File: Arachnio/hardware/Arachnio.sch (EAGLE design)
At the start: 62 parts, among them J5 HEAD17-NOSS, J6 HEAD17-NOSS, Q1 8MHz, T1 FDN340P/PMV48XP, U1 ATMEGA32U4-XUMU, U2 AP2111HA-3.3, U3 ZLDO1117-5.0, U5 ESP8266EX, U6 SPI_FLASH, Y1 26 MHz/10 pF

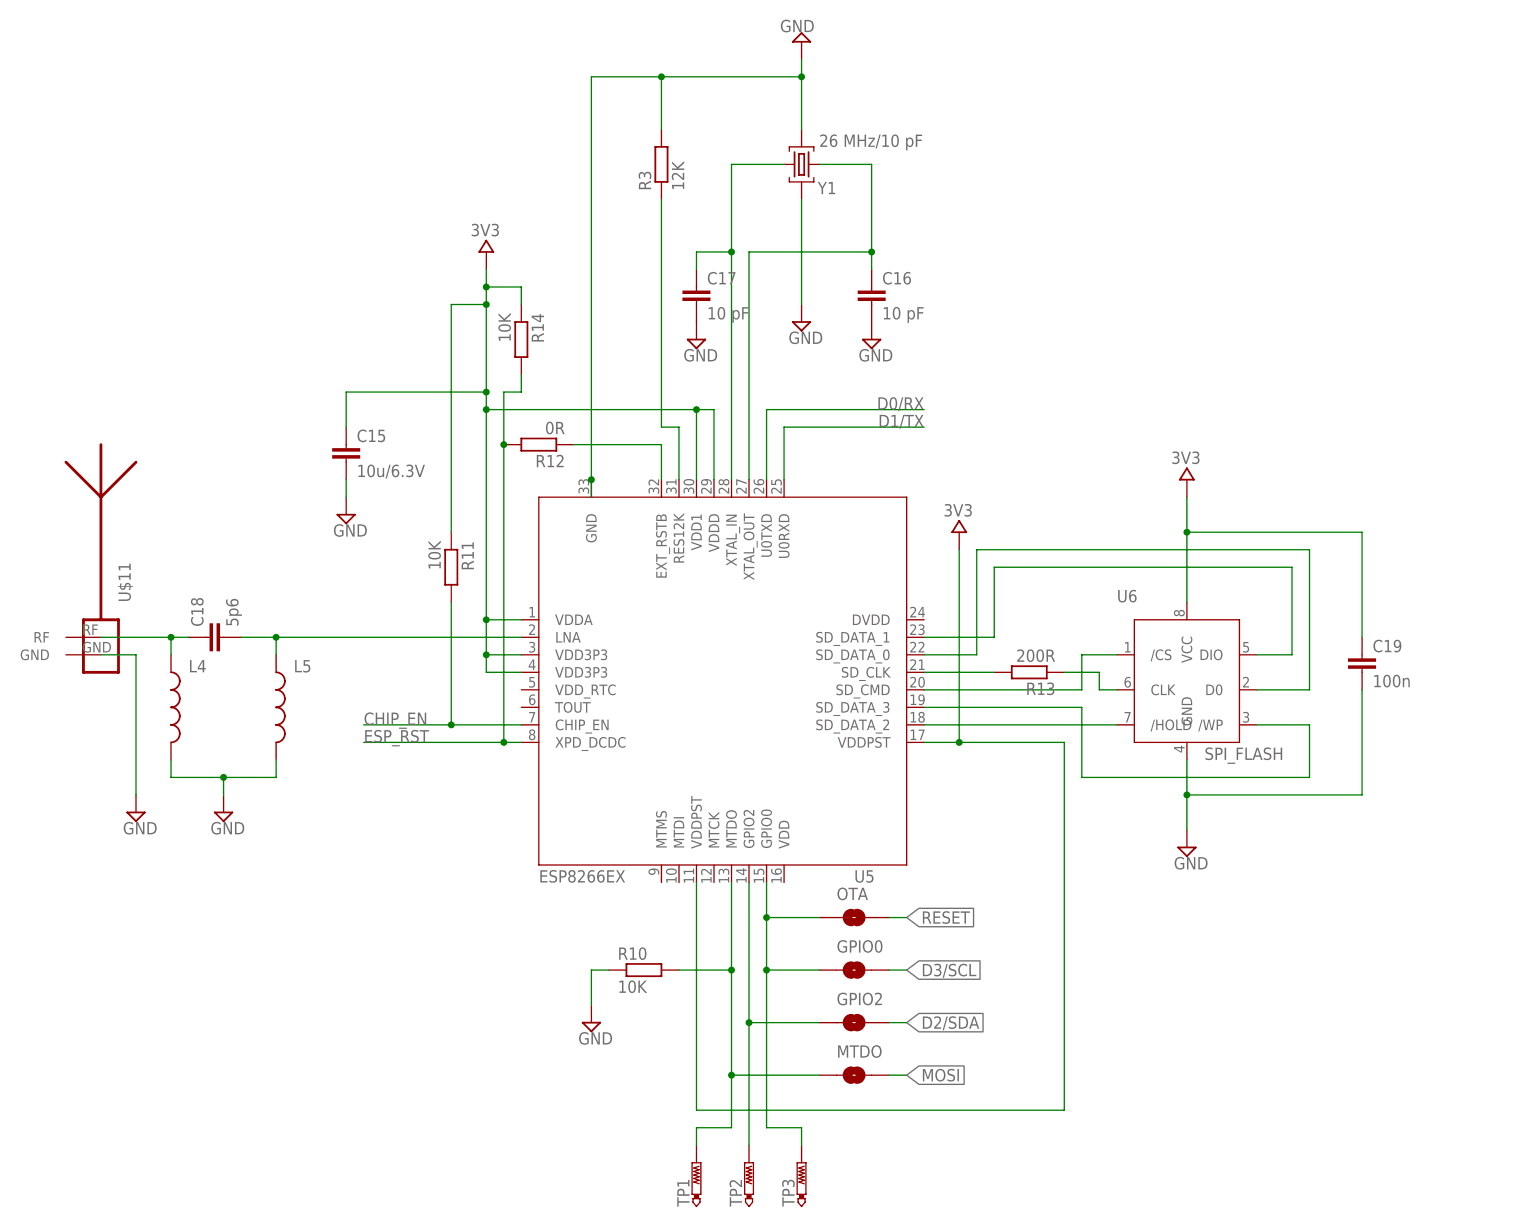
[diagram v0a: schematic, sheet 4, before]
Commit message: ﻿Added 3 new decoupling caps to the ESP8266 # Please enter the commit message for your changes. Lines starting # with '#' will be ignored, and an empty message aborts the commit. # On branch decoupling # Changes to be committed: #	modified:   Arachnio/hardware/Arachnio.brd #	modified:   Arachnio/hardware/Arachnio.sch #
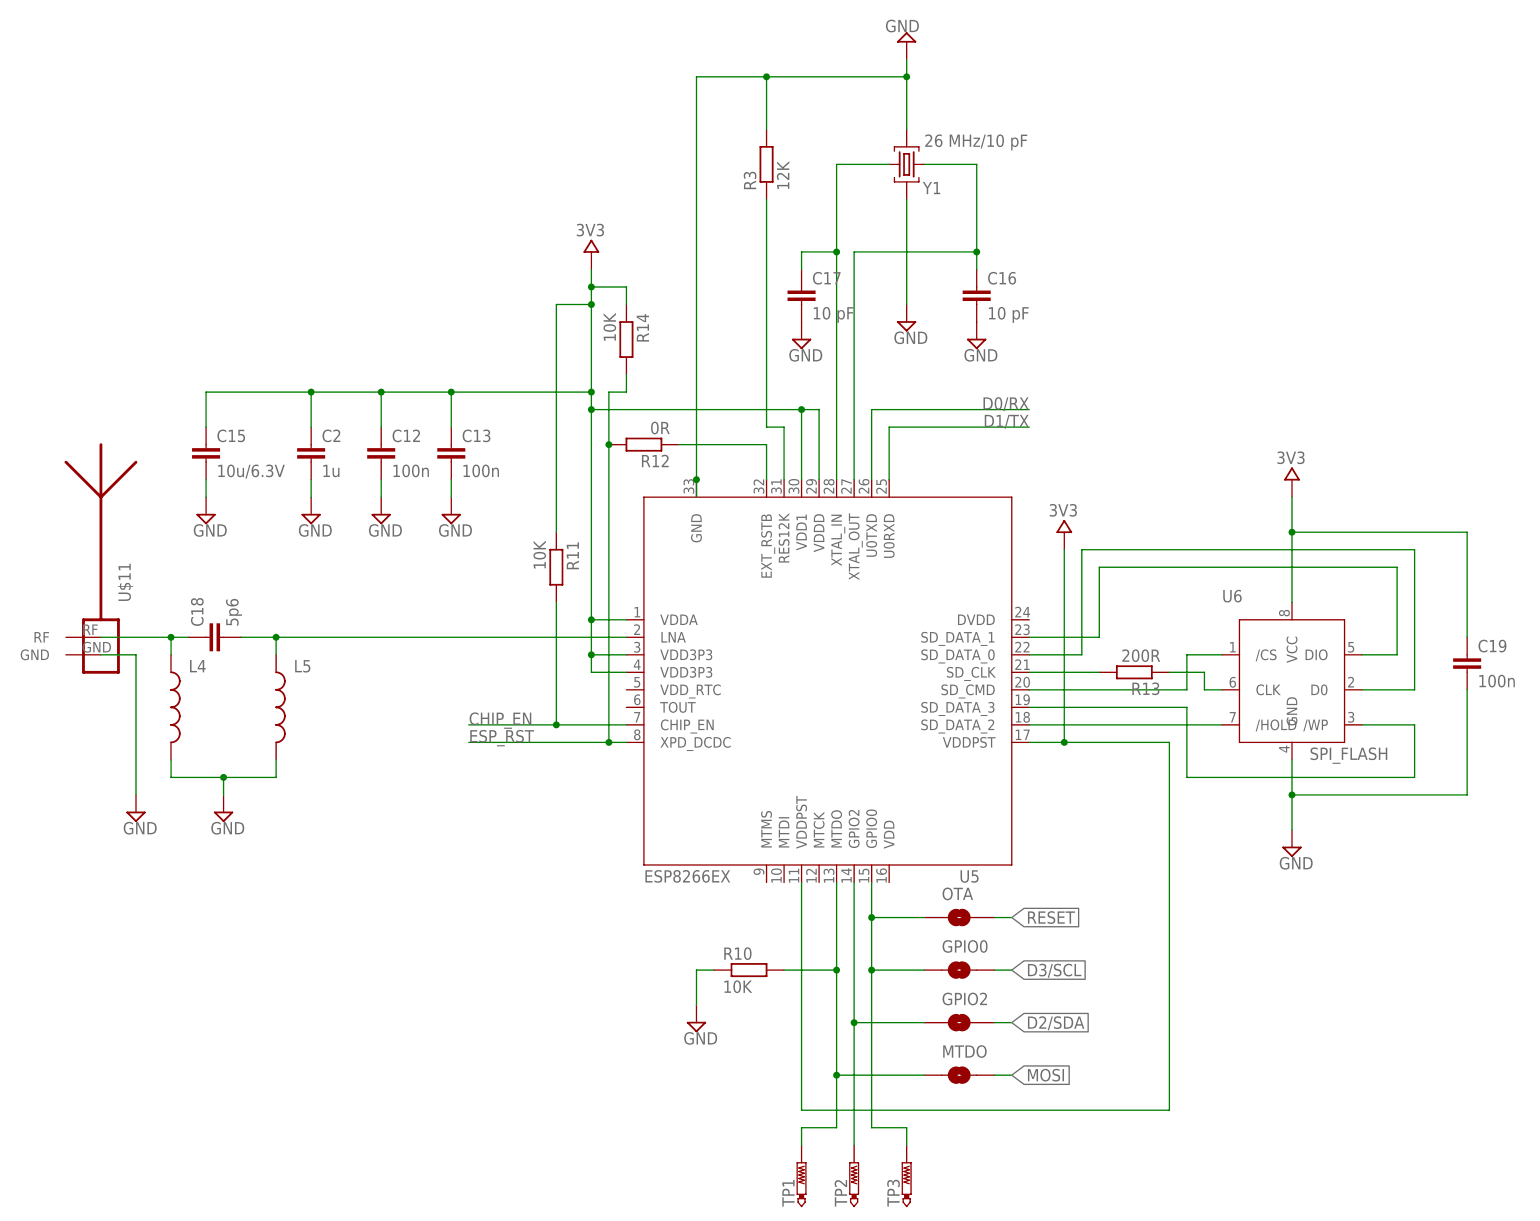
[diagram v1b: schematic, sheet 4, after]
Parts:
- added C12, C13: 100n, resistor:C-EUC0603
- added C2: 1u, resistor:C-EUC0603
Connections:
- net 3V3: now also C12.1, C13.1, C2.1
- net GND: now also C12.2, C13.2, C2.2
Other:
- moved on the sheet: C15, C16, C17, C19, GPIO0, GPIO2, MTDO, OTA, R10, R11, R12, R13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

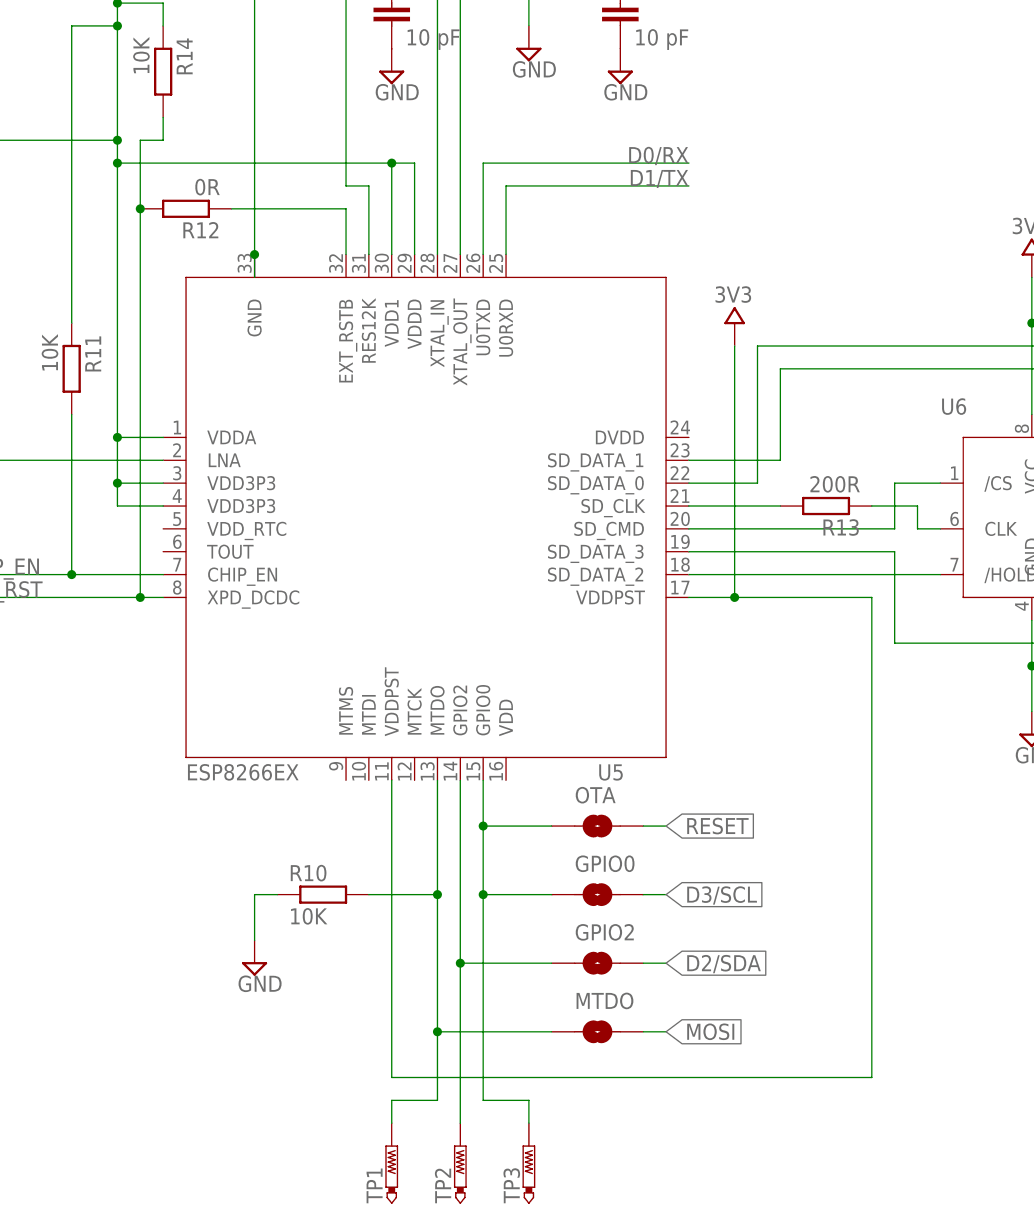
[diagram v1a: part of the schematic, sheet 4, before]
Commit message: -- Fixed ground plane issues -- Connected USB shield to ground -- Simplified boot select by tying MTDO and GPIO2 low and high, respectively -- Removed test points for MTDO and GPIO2 -- Replaced 0R resistor with NC by trace solder jumper -- Replaced GPIO2 and OTA jumpers with a single 3-way NO solder jumper
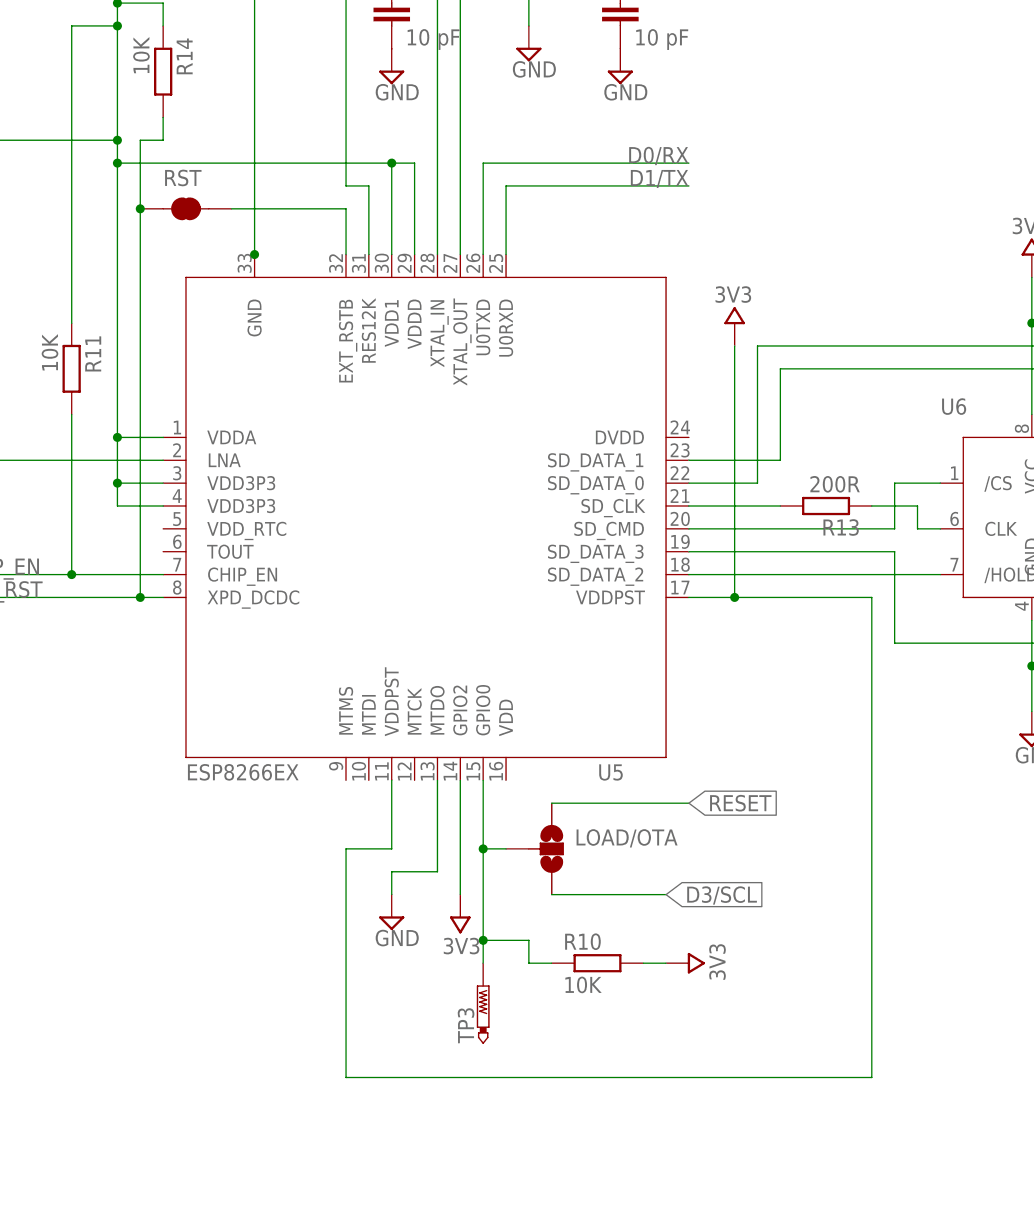
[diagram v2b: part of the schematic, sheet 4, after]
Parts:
- removed GPIO0, GPIO2, MTDO, OTA: JUMPER-PAD-2-NOYES_SILK, SparkFun-Passives:JUMPER-PAD-2-NOYES_SILK
- removed R12: 0R, resistor:R-EU_R0603
- removed TP1, TP2: PTR1TP15SQ, testpad:PTR1TP15SQ
- added LOAD/OTA: JUMPER-PAD-3-NOYES_SILK, SparkFun-Passives:JUMPER-PAD-3-NOYES_SILK
- added RST: JUMPER-PAD-2-NC_BY_TRACE, SparkFun-Passives:JUMPER-PAD-2-NC_BY_TRACE
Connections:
- removed net N$1: MTDO.1, R10.2, TP1.TP, U5.MTDO
- removed net N$5: GPIO2.1, TP2.TP, U5.GPIO2
- net 3V3: now also R10.2, U5.GPIO2
- net D2/SDA: no longer GPIO2.2
- net D3/SCL: now also LOAD/OTA.3; no longer GPIO0.2
- net ESP_RST: now also RST.1; no longer R12.2
- net GND: now also CN1.SHIELD@0, CN1.SHIELD@1, CN1.SHIELD@2, CN1.SHIELD@3, U5.MTDO; no longer R10.1
- net MOSI: no longer MTDO.2
- net N$33: now also RST.2; no longer R12.1
- net N$6: now also LOAD/OTA.2, R10.1; no longer GPIO0.1, OTA.1
- net RESET: now also LOAD/OTA.1; no longer OTA.2
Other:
- moved on the sheet: CN1, F1, R10, TP3
